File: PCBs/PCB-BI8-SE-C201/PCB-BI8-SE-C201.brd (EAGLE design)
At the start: 87.6 x 55.9 mm, 36 parts, among them IC1 MCP23017SS, IC2 PCA9685

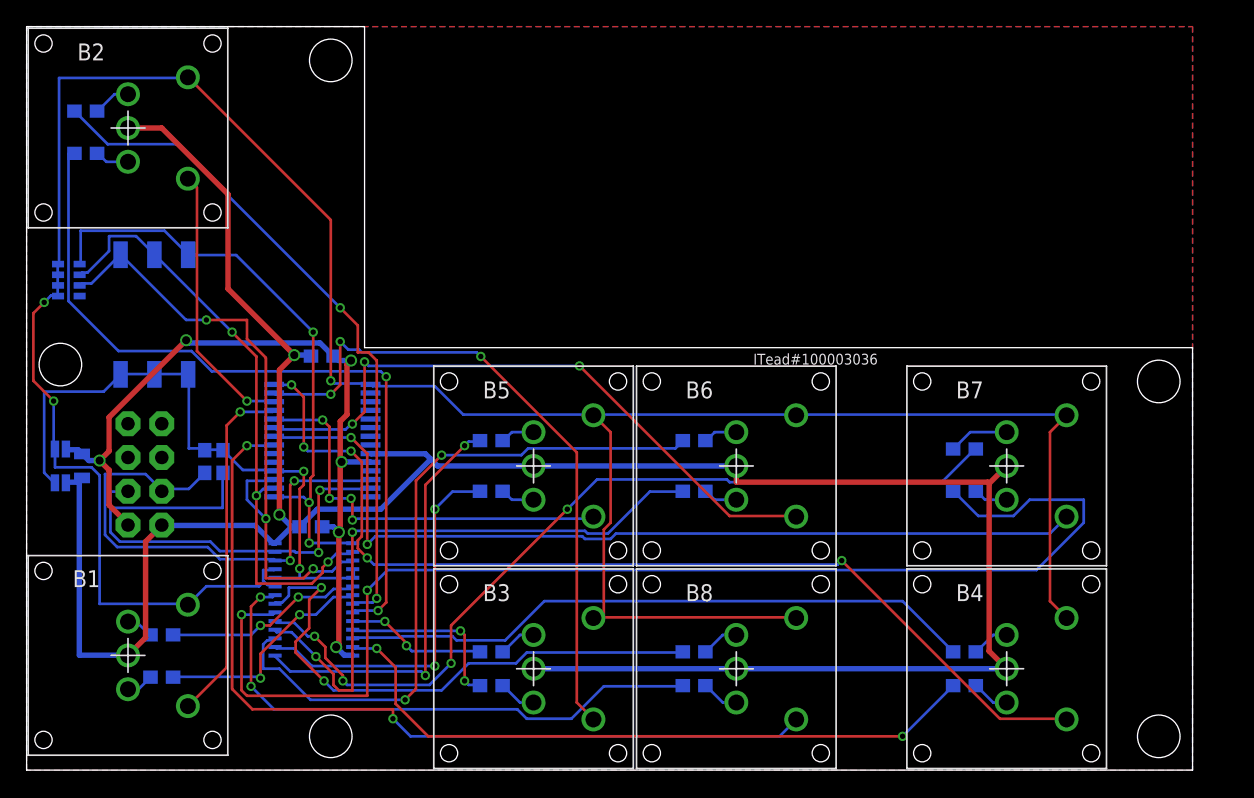
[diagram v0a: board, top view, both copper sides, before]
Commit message: Large revisions of boards, change of forms, in particular all mounting holes now has a 7mm diameter and fully inside the board.
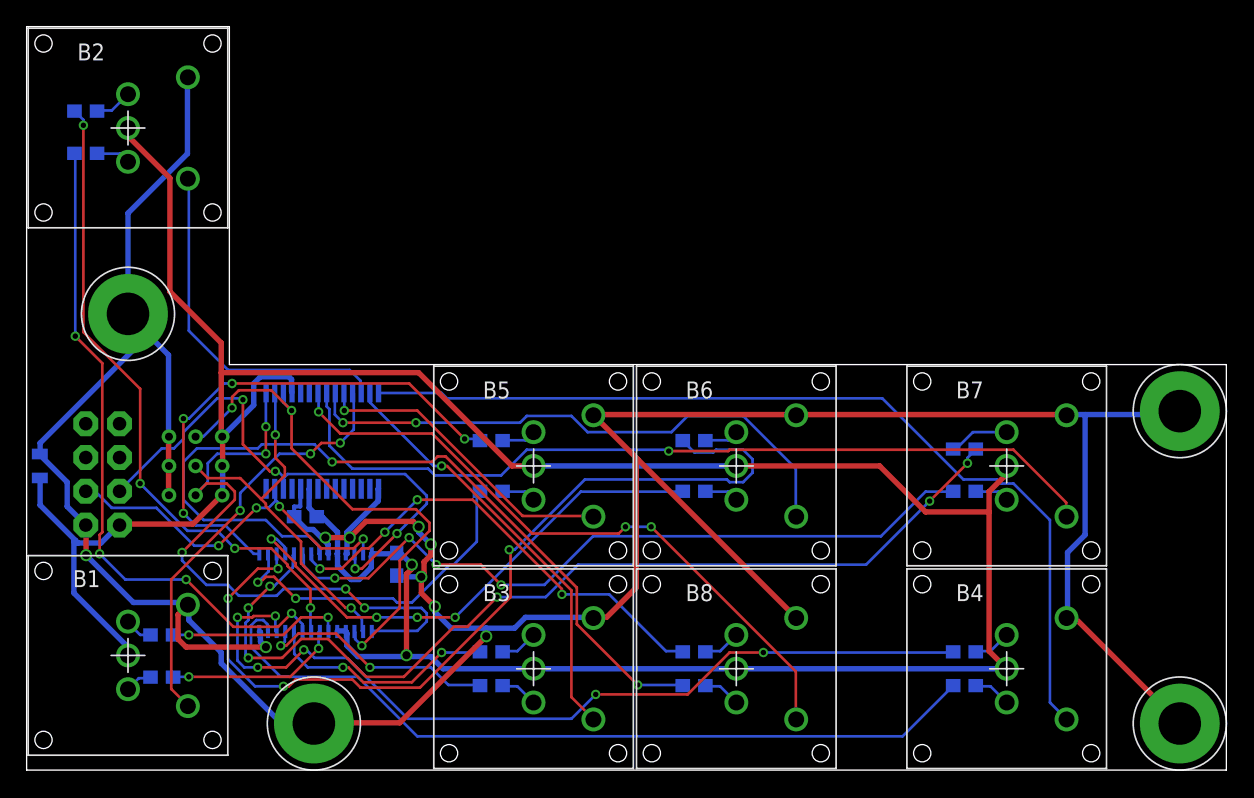
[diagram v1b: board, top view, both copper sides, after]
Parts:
- removed R1, R2: 10K, SparkFun:0603-RES
- removed RN1: 10K, SKAARHOJ:CAY16_HAND
- removed S2: SWS003, smd-special:SMS-003
- removed SJ1, SJ2: SOLDERJUMPERNC, SparkFun:SJ_2S
- added U$15, U$18, U$20, U$21: GNDPAD6MM, SKAARHOJ:3.2MMPAD6MM
- added U$19: 3BITADDR, SKAARHOJ:3BITADDR
- moved C1 12.1 mm to (21.0, 19.1), turned to 180 degrees
- moved C2 7.04 mm to (27.8, 15.5), turned to 270 degrees
- moved SERIAL 3.18 mm to (5.71, 22.2)
- moved C3 3.18 mm to (0.99, 22.9)
- moved IC2 0.52 mm to (21.7, 13.3), turned to 0 degrees
- turned IC1 to 0 degrees
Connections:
- removed net 5VL: IC1.18, IC2.24, IC2.4, IC2.5, R1.1, R2.1, S2.1, S2.2, S2.3, SJ1.2
- removed net GNDL: B1.P$4, B2.P$4, B3.P$4, B4.P$4, B5.P$4, B6.P$4, B7.P$4, B8.P$4, IC1.1, IC2.23, IC2.25, RN1.1, RN1.2, RN1.3, RN1.4, SJ2.2
- net 5V: now also IC1.18, IC2.24, IC2.4, IC2.5, U$19.H1, U$19.H2, U$19.H3; no longer SJ1.1
- net A0: now also U$19.A0; no longer RN1.5, S2.6
- net A1: now also U$19.A1; no longer RN1.6, S2.5
- net A2: now also U$19.A2; no longer RN1.7, S2.4
- net GND: now also B1.P$4, B2.P$4, B3.P$4, B4.P$4, B5.P$4, B6.P$4, B7.P$4, B8.P$4, IC1.1, IC2.23, IC2.25, U$15.P$1, U$18.P$1, U$19.L1, U$19.L2, U$19.L3, U$20.P$1, U$21.P$1; no longer SJ2.1
- net I2C_SCL: no longer R2.2
- net I2C_SDA: no longer R1.2
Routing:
- net GNDL: track 202.0 -> 0.00 mm, vias 3 -> 0
- net GND: track 60.6 -> 259.4 mm, vias 6 -> 9
- net 5VL: track 48.4 -> 0.00 mm, vias 2 -> 0
- net N$25: track 94.6 -> 55.8 mm, vias 2 -> 4
- net 5V: track 191.1 -> 220.7 mm
- net N$27: track 42.6 -> 62.7 mm
- net GPA6: track 50.4 -> 32.1 mm, vias 3 -> 1
- net N$5: track 48.1 -> 66.1 mm, vias 0 -> 6
- net A1: track 46.0 -> 28.4 mm, vias 3 -> 2
- net GPA0: track 65.7 -> 49.5 mm, vias 2 -> 3
- net N$22: track 52.7 -> 67.2 mm, vias 2 -> 4
- net I2C_SDA: track 40.4 -> 27.9 mm, vias 2 -> 4
- net N$4: track 51.1 -> 60.9 mm, vias 2 -> 0
- net N$24: track 64.6 -> 73.4 mm, vias 4 -> 6
- net A2: track 48.3 -> 39.6 mm
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- removed copper zone on layer 1, net GND
- removed copper zone on layer 16, net GND
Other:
- board size 87.6 x 55.9 mm -> 90.2 x 55.9 mm
- board text added: "GITHUB: SKAARHOJ-Open-Engineering"
- board text added: "SKAARHOJ 2013"
- board text removed: "5V"
- board text removed: "GND"
- board text removed: "ITead#100003036"
- board text removed: "SKAARHOJ 2012"
- board text removed: "https://github.com/kasperskaarhoj/SKAARHOJ-Open-Engineering"

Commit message: Boards
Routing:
- added copper zone on layer 1, net GND
- added copper zone on layer 16, net GND
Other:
- board text added: "v07-13"
- board text removed: "v02-10-12"

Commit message: asdf
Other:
- board text added: "v09-13"
- board text removed: "v07-13"
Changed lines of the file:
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@@
 <?xml version="1.0" encoding="utf-8"?>
 <!DOCTYPE eagle SYSTEM "eagle.dtd">
-<eagle version="6.4">
+<eagle version="6.5.0">
 <drawing>
 <settings>
@@
 <layer number="14" name="Route14" color="1" fill="6" visible="no" active="no"/>
 <layer number="15" name="Route15" color="4" fill="6" visible="no" active="no"/>
-<layer number="16" name="Bottom" color="1" fill="1" visible="no" active="yes"/>
+<layer number="16" name="Bottom" color="1" fill="1" visible="yes" active="yes"/>
 <layer number="17" name="Pads" color="2" fill="1" visible="yes" active="yes"/>
 <layer number="18" name="Vias" color="2" fill="1" visible="yes" active="yes"/>
@@
 <text x="7.7978" y="20.193" size="0.8128" layer="122" rot="MR90">SCL</text>
 <text x="3.175" y="18.415" size="1.778" layer="122" rot="MR270">1</text>
-<text x="85.09" y="17.653" size="0.8128" layer="122" rot="MR270">v07-13</text>
+<text x="85.09" y="17.653" size="0.8128" layer="122" rot="MR270">v09-13</text>
 <text x="63.8175" y="2.286" size="0.8128" layer="122" font="vector" rot="MR0">GITHUB: SKAARHOJ-Open-Engineering</text>
 <wire x1="90.17" y1="30.48" x2="15.24" y2="30.48" width="0" layer="20"/>

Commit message: PCBS updated
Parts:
- removed C3: 10uF, SparkFun:0805
- added C4: 22uF, SparkFun:0805
- added C5, C6, C7, C8: 100nF, SparkFun:0603-CAP
- added L4: ILHB0805ER121V, SparkFun:0805
- moved C2 1.06 mm to (28.3, 16.4), turned to 180 degrees
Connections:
- new net N$1: C6.1, L4.1, SERIAL.2
- net 5V: now also C4.1, C5.1, C7.1, C8.1, L4.2; no longer C3.1, SERIAL.2
- net GND: now also C4.2, C5.2, C6.2, C7.2, C8.2; no longer C3.2
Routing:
- net N$4: track 60.9 -> 162.3 mm, vias 0 -> 2
- net 5V: track 220.7 -> 257.3 mm, vias 2 -> 5
- net N$22: track 67.2 -> 37.9 mm
- net A2: track 39.6 -> 65.4 mm, vias 3 -> 2
- net N$25: track 55.8 -> 79.4 mm, vias 4 -> 2
- net N$27: track 62.7 -> 40.6 mm, vias 2 -> 4
- net N$21: track 25.8 -> 47.2 mm
- net N$23: track 39.2 -> 57.9 mm, vias 4 -> 6
- net GPA4: track 32.0 -> 47.3 mm, vias 3 -> 1
- net N$20: track 39.2 -> 24.9 mm, vias 4 -> 2
- net N$11: track 49.4 -> 60.9 mm, vias 4 -> 0
- net A0: track 48.0 -> 59.0 mm, vias 5 -> 4
- net N$24: track 73.4 -> 63.1 mm, vias 6 -> 4
- net GND: track 259.4 -> 249.2 mm, vias 9 -> 5
- net N$5: track 66.1 -> 57.5 mm, vias 6 -> 2
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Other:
- board text added: "SKAARHOJ 2014"
- board text added: "v10-14"
- board text removed: "SCL"
- board text removed: "SDA"
- board text removed: "SKAARHOJ 2013"
- board text removed: "v09-13"

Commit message: PCB updates
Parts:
- SERIAL: value M04X2 -> M04X2M2X4SMALLER; device SparkFun:2X4 -> SKAARHOJ:M2X4SMALLER
- U$19: value 3BITADDR -> 3BITADDRSMALL; device SKAARHOJ:3BITADDR -> SKAARHOJ:3BITADDR_SMALL
- turned SERIAL to 180 degrees
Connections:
- net 5V: now also U$19.H0; no longer U$19.H3
- net A0: now also U$19.AS0
- net A1: now also U$19.AS1
- net A2: now also U$19.AS2
- net GND: now also U$19.L0; no longer U$19.L3
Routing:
- net GND: track 249.2 -> 272.4 mm, vias 5 -> 6
- net I2C_SCL: track 50.0 -> 45.2 mm, vias 2 -> 3
- net A1: track 34.5 -> 29.7 mm, vias 2 -> 3
- net A0: track 59.0 -> 55.9 mm, vias 4 -> 5
- net A2: track 65.4 -> 66.5 mm
- net 5V: track 257.3 -> 256.4 mm, vias 5 -> 6
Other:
- board text added: "BI8-SE-C201, v02-16"
- board text removed: "1"
- board text removed: "BI8-SE-C201"
- board text removed: "GITHUB: SKAARHOJ-Open-Engineering"
- board text removed: "SKAARHOJ 2014"
- board text removed: "v10-14"
